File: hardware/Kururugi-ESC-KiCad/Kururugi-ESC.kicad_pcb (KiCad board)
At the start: 6 copper layers, 37.9 x 23.6 mm, 141 parts, among them J1 Conn_01x01, J10 Conn_01x01, J11 Conn_01x01, J2 Conn_01x01, J3 Conn_01x01, J4 Conn_01x01, J5 Conn_01x01, J6 Conn_01x01, J7 Conn_01x01, J8 JTAG_TC2030, J9 Conn_01x01, Q1 CSD18540Q5B, Q2 CSD18540Q5B, Q3 CSD18540Q5B, Q4 CSD18540Q5B, Q5 CSD18540Q5B, Q6 CSD18540Q5B, U1 STM32G474CEU6, U2 LM5160A, U3 TPS7B92033, U4 2EDL8024, U5 2EDL8024, U6 2EDL8024, X1 16MHz

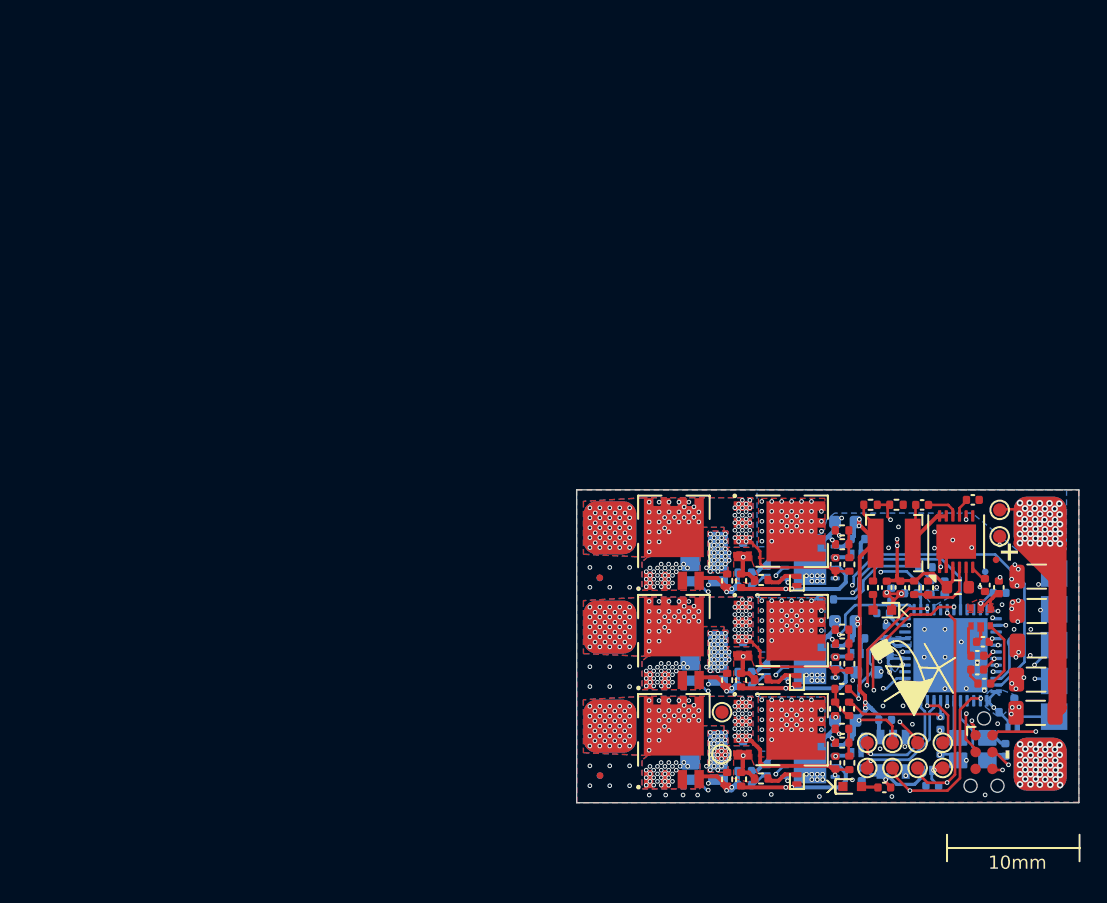
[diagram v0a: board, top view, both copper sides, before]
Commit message: PCB view improvments
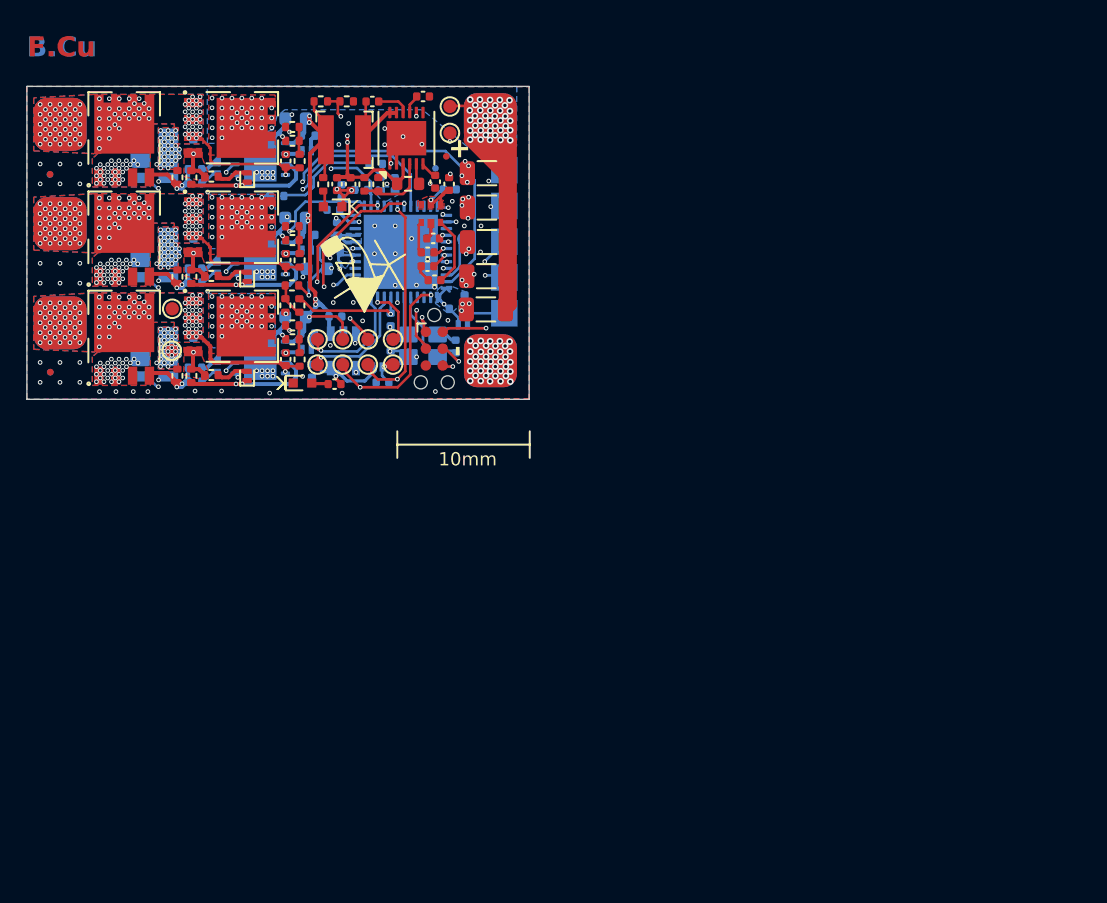
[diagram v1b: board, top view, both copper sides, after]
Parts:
- moved Q4 51.5 mm to (55.3, 35.9)
- moved R36 51.5 mm to (57.6, 37.1)
- moved C1 51.5 mm to (82.7, 30.8)
- moved C10 51.5 mm to (71.3, 31.7)
- moved C11 51.5 mm to (72.4, 31.7)
- moved C13 51.5 mm to (77.8, 25.0)
- moved C14 51.5 mm to (78.8, 31.5)
- moved C15 51.5 mm to (80.3, 41.1)
- moved C16 51.5 mm to (71.3, 35.0)
- moved C17 51.5 mm to (69.8, 38.1)
- moved C19 51.5 mm to (80.3, 43.9)
- moved C2 51.5 mm to (82.7, 33.4)
- moved C22 51.5 mm to (71.2, 41.6)
- moved C24 51.5 mm to (79.8, 31.6)
- moved C25 51.5 mm to (67.5, 29.9)
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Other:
- board text added: "B.Cu"
- board text added: "Edge.Cuts"
- board text added: "F.Cu"
- board text added: "In1.Cu"
- board text added: "In2.Cu"
- board text added: "In3.Cu"
- board text added: "In4.Cu"

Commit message: PCB Improvments
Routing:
- net VBAT: track 56.9 -> 51.5 mm, vias 142 -> 143
- added copper zone on F.Cu, net /SW
- added copper zone on F.Cu, net VBUCK
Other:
- outline, holes or cut-outs redrawn
- board text removed: "Edge.Cuts"
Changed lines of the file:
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@@
 		(layer "F.SilkS")
 	)
-	(gr_rect
-		(start 47.948628 24.289474)
-		(end 85.848628 47.902474)
+	(gr_line
+		(start 49.948628 24.289474)
+		(end 83.848628 24.289474)
+		(stroke
+			(width 0.05)
+			(type default)
+		)
+		(layer "Edge.Cuts")
+	)
+	(gr_arc
+		(start 47.948628 26.289474)
+		(mid 48.534425 24.875287)
+		(end 49.948628 24.289474)
+		(stroke
+			(width 0.05)
+			(type default)
+		)
+		(layer "Edge.Cuts")
+	)
+	(gr_arc
+		(start 83.848628 24.289474)
+		(mid 85.262842 24.87526)
+		(end 85.848628 26.289474)
+		(stroke
+			(width 0.05)
+			(type default)
+		)
+		(layer "Edge.Cuts")
+	)
+	(gr_arc
+		(start 85.848628 45.902474)
+		(mid 85.262852 47.316714)
+		(end 83.848628 47.902474)
+		(stroke
+			(width 0.05)
+			(type default)
+		)
+		(layer "Edge.Cuts")
+	)
+	(gr_line
+		(start 85.848628 26.289474)
+		(end 85.848628 45.902474)
+		(stroke
+			(width 0.05)
+			(type default)
+		)
+		(layer "Edge.Cuts")
+	)
+	(gr_arc
+		(start 49.948628 47.902474)
+		(mid 48.534414 47.316688)
+		(end 47.948628 45.902474)
+		(stroke
+			(width 0.05)
+			(type default)
+		)
+		(layer "Edge.Cuts")
+	)
+	(gr_line
+		(start 83.848628 47.902474)
+		(end 49.948628 47.902474)
+		(stroke
+			(width 0.05)
+			(type default)
+		)
+		(layer "Edge.Cuts")
+	)
+	(gr_line
+		(start 47.948628 45.902474)
+		(end 47.948628 26.289474)
 		(stroke
 			(width 0.05)
 			(type default)
 		)
-		(fill no)
 		(layer "Edge.Cuts")
 	)
 	(gr_text "F.Cu"
-		(at 47.97 22.2 0)
+		(at 48 23.26 0)
 		(layer "F.Cu")
 		(effects
@@
 	)
 	(gr_text "B.Cu"
-		(at 47.92 22.2 0)
+		(at 47.95 23.26 0)
 		(layer "B.Cu")
 		(effects
@@
 	)
 	(gr_text "In1.Cu"
-		(at 47.92 22.2 0)
+		(at 47.95 23.26 0)
 		(layer "In1.Cu")
 		(effects
@@
 	)
 	(gr_text "In2.Cu"
-		(at 47.92 22.2 0)
+		(at 47.95 23.26 0)
 		(layer "In2.Cu")
 		(effects
@@
 	)
 	(gr_text "-"
-		(at 81.588628 45.499474 90)
+		(at 81.42 45.55 90)
 		(layer "B.SilkS")
 		(effects
@@
 	)
 	(gr_text "In3.Cu"
-		(at 47.92 22.2 0)
+		(at 47.95 23.26 0)
 		(layer "In3.Cu")
 		(effects
@@
 	)
 	(gr_text "In4.Cu"
-		(at 47.92 22.2 0)
+		(at 47.95 23.26 0)
 		(layer "In4.Cu")
 		(effects
@@
 		)
 	)
-	(gr_text "Edge.Cuts"
-		(at 47.92 22.2 0)
-		(layer "Edge.Cuts")
-		(effects
-			(font
-				(size 1.5 1.5)
-				(thickness 0.3)
-				(bold yes)
-			)
-			(justify left bottom)
-		)
-	)
 	(segment
 		(start 69.258628 26.539474)
@@
 	)
 	(via
-		(at 75.428628 30.099474)
+		(at 75.337628 30.136974)
 		(size 0.35)
 		(drill 0.2)
@@
 	)
 	(segment
-		(start 72.136628 30.719474)
-		(end 72.136628 30.971474)
-		(width 0.25)
-		(layer "F.Cu")
-		(net 9)
-	)
-	(segment
 		(start 84.420828 28.357837)
 		(end 84.420828 40.752274)
@@
 	)
 	(segment
-		(start 73.564878 31.142224)
-		(end 74.107628 30.599474)
-		(width 0.25)
-		(layer "F.Cu")
-		(net 9)
-	)
-	(segment
 		(start 84.136628 30.497474)
 		(end 82.118628 28.479474)
@@
 	)
 	(segment
+		(start 76.37 31.74)
+		(end 76.18 31.93)
+		(width 0.2)
+		(layer "F.Cu")
+		(net 9)
+	)
+	(segment
 		(start 71.459378 31.142224)
 		(end 73.564878 31.142224)
@@
 	)
 	(segment
-		(start 72.136628 28.025474)
-		(end 72.136628 30.719474)
-		(width 0.25)
-		(layer "F.Cu")
-		(net 9)
-	)
-	(segment
 		(start 84.136628 30.840437)
 		(end 84.136628 28.642037)
@@
 	)
 	(segment
-		(start 74.847628 30.599474)
-		(end 75.887628 31.639474)
-		(width 0.25)
-		(layer "F.Cu")
-		(net 9)
-	)
-	(segment
 		(start 75.887628 31.639474)
 		(end 75.988628 31.639474)
@@
 	)
 	(segment
-		(start 74.107628 30.599474)
-		(end 74.847628 30.599474)
-		(width 0.25)
-		(layer "F.Cu")
-		(net 9)
-	)
-	(segment
-		(start 72.136628 30.971474)
-		(end 71.978628 31.129474)
-		(width 0.25)
-		(layer "F.Cu")
-		(net 9)
-	)
-	(segment
-		(start 72.129628 28.018474)
-		(end 72.136628 28.025474)
-		(width 0.25)
+		(start 76.18 31.93)
+		(end 76.17 31.93)
+		(width 0.2)
 		(layer "F.Cu")
 		(net 9)
@@
 	)
 	(segment
-		(start 72.136628 30.895474)
-		(end 72.407378 31.166224)
+		(start 72.86 31.142224)
+		(end 72.559378 31.142224)
 		(width 0.25)
 		(layer "F.Cu")
@@
 	)
 	(segment
+		(start 76.36 31.29)
+		(end 76.36 31.56)
+		(width 0.2)
+		(layer "F.Cu")
+		(net 9)
+	)
+	(segment
 		(start 84.420828 40.752274)
 		(end 84.056628 41.116474)
@@
 	)
 	(segment
+		(start 76.36 31.56)
+		(end 76.280526 31.639474)
+		(width 0.2)
+		(layer "F.Cu")
+		(net 9)
+	)
+	(segment
 		(start 71.459378 31.142224)
 		(end 71.425378 31.176224)
@@
 	)
 	(segment
-		(start 71.472128 31.129474)
-		(end 71.425378 31.176224)
-		(width 0.25)
+		(start 76.280526 31.639474)
+		(end 75.888628 31.639474)
+		(width 0.2)
 		(layer "F.Cu")
 		(net 9)
 	)
 	(segment
-		(start 72.136628 30.719474)
-		(end 72.136628 30.895474)
+		(start 71.472128 31.129474)
+		(end 71.425378 31.176224)
 		(width 0.25)
 		(layer "F.Cu")
@@
 	)
 	(via
+		(at 76.37 31.74)
+		(size 0.35)
+		(drill 0.2)
+		(layers "F.Cu" "B.Cu")
+		(net 9)
+	)
+	(via
 		(at 62.668413 35.659744)
 		(size 0.35)
@@
 	)
 	(via
-		(at 72.129628 28.018474)
-		(size 0.35)
-		(drill 0.2)
-		(layers "F.Cu" "B.Cu")
-		(net 9)
-	)
-	(via
 		(at 61.926703 43.141696)
 		(size 0.35)
@@
 	)
 	(via
+		(at 76.36 31.29)
+		(size 0.35)
+		(drill 0.2)
+		(layers "F.Cu" "B.Cu")
+		(net 9)
+	)
+	(via
 		(at 84.044628 26.534874)
 		(size 0.5)
@@
 	)
 	(via
-		(at 72.138628 28.509474)
+		(at 72.378628 31.179474)
 		(size 0.35)
 		(drill 0.2)
@@
 	)
 	(segment
-		(start 75.140628 26.291974)
-		(end 75.712628 26.291974)
+		(start 73.311628 28.120974)
+		(end 73.311628 28.312974)
+		(width 0.5)
+		(layer "F.Cu")
+		(net 16)
+	)
+	(segment
+		(start 73.311628 27.738372)
+		(end 73.311628 28.120974)
 		(width 0.3)
 		(layer "F.Cu")
@@
 	)
 	(segment
-		(start 73.311628 28.120974)
-		(end 73.311628 28.312974)
-		(width 0.5)
+		(start 75.712628 26.291974)
+		(end 74.758026 26.291974)
+		(width 0.3)
 		(layer "F.Cu")
 		(net 16)
@@
 	)
 	(segment
-		(start 75.140628 26.291974)
-		(end 73.311628 28.120974)
+		(start 74.758026 26.291974)
+		(end 73.311628 27.738372)
 		(width 0.3)
 		(layer "F.Cu")
@@
 	)
 	(zone
+		(net 16)
+		(net_name "/SW")
+		(layer "F.Cu")
+		(hatch edge 0.5)
+		(priority 14)
+		(connect_pads yes
+			(clearance 0)
+		)
+		(min_thickness 0.25)
+		(filled_areas_thickness no)
+		(fill yes
+			(thermal_gap 0.5)
+			(thermal_bridge_width 0.5)
+		)
+		(polygon
+			(pts
+				(xy 73.54 25.5) (xy 73.38 27.59) (xy 74.1 26.96) (xy 74.8 26.3) (xy 74.83 26.22) (xy 73.65 25.28)
+			)
+		)
+	)
+	(zone
 		(net 78)
 		(net_name "/PHASE 1/GH")
@@
 			)
 		)
+	)
+	(zone
+		(net 1)
+		(net_name "VBUCK")
+		(layer "F.Cu")
+		(hatch edge 0.5)
+		(priority 15)
+		(connect_pads yes
+			(clearance 0)
+		)
+		(min_thickness 0.25)
+		(filled_areas_thickness no)
+		(fill yes
+			(thermal_gap 0.5)
+			(thermal_bridge_width 0.5)
+		)
+		(polygon
+			(pts
+				(xy 69.35 25.74) (xy 69.08 26.48) (xy 69.08 27.02) (xy 69.16 31.44) (xy 69.16 32.69) (xy 70.63 31.44)
+				(xy 71.12 30.16) (xy 71.12 26.46) (xy 69.89 25.1) (xy 69.35 25.1)
+			)
+		)
